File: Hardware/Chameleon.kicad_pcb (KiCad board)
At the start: 2 copper layers, 88 x 88 mm, 72 parts, among them P1 PDI, U1 ATXMEGA16A4U-A, U2 AS1121, U3 TLV71333PDBVR, U4 NCP1402

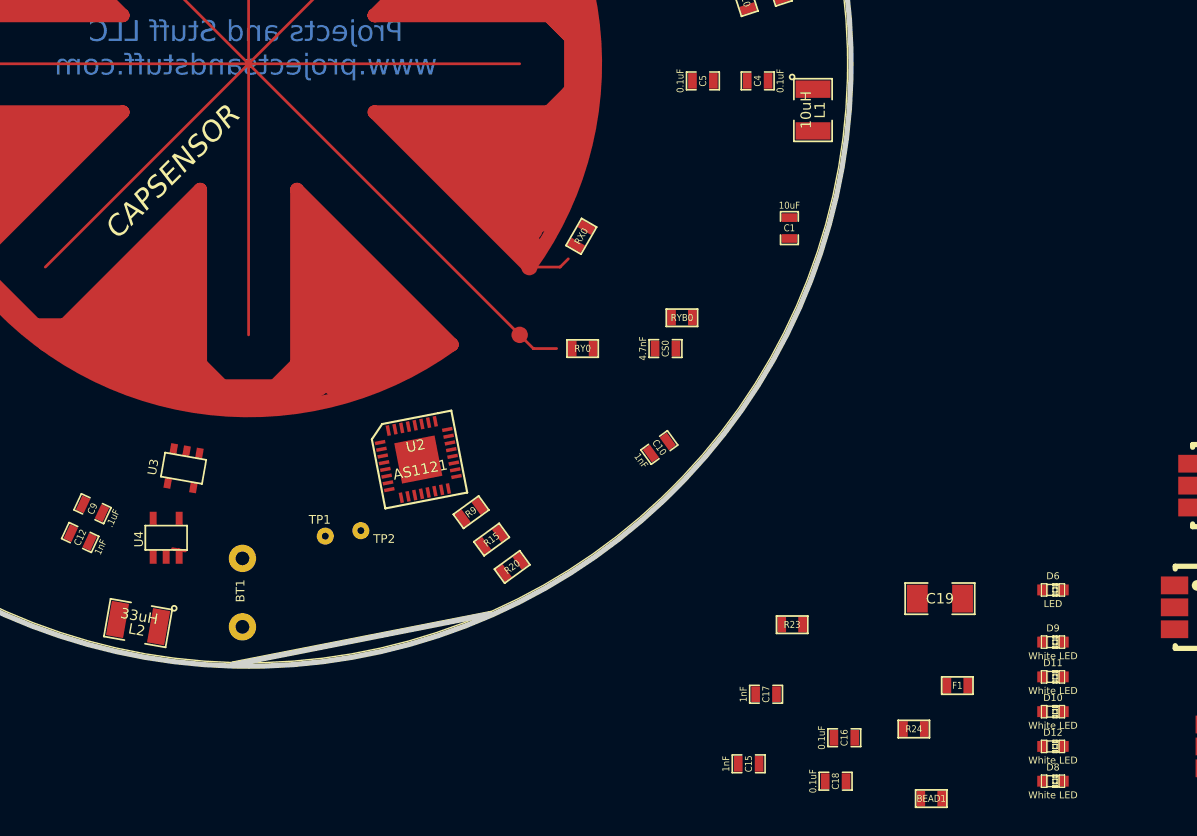
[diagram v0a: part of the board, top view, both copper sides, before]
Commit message: Created netlist and imported components into PCB
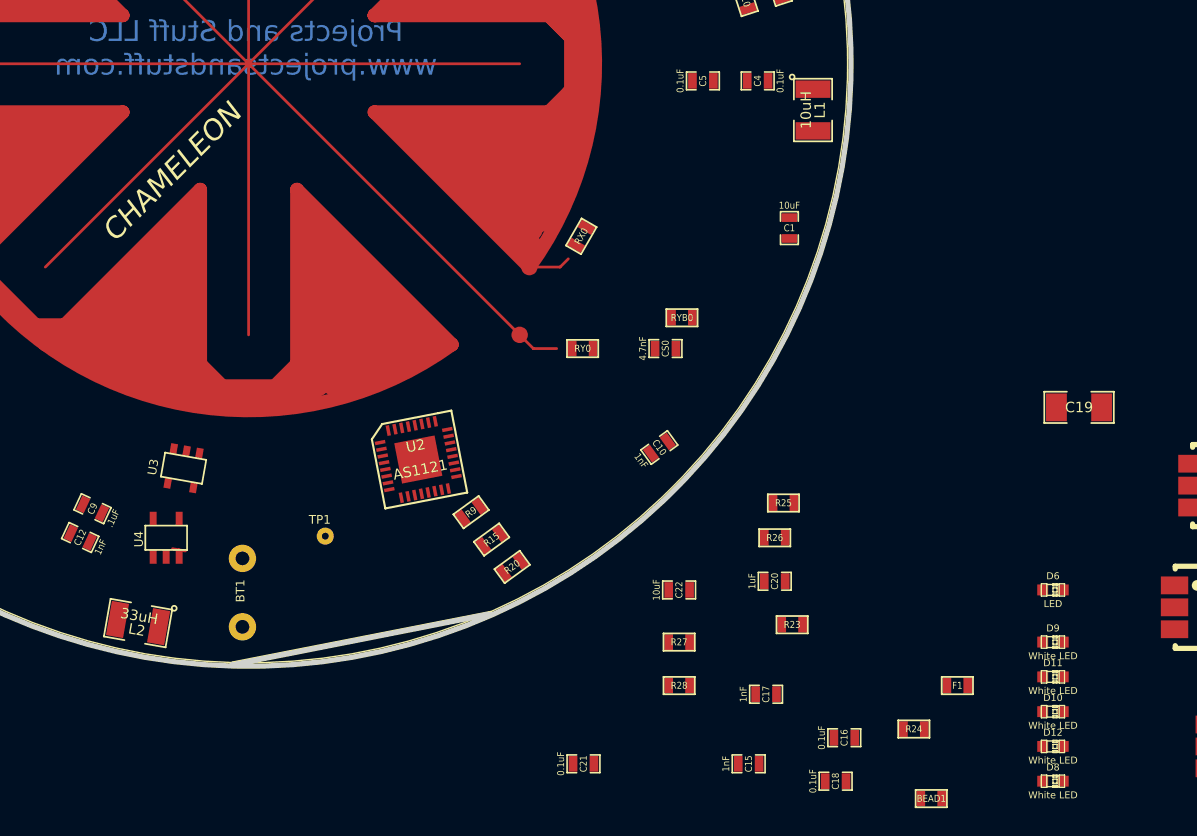
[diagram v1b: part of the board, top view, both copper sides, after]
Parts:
- removed TP2: TST, TestPoint_1-pin
- added C20: 1uF, SM0603_Capa, F.Cu at (138.4, 137.8)
- added C21: 0.1uF, SM0603_Capa, F.Cu at (124.5, 151.1)
- added C22: 10uF, SM0603_Capa, F.Cu at (131.4, 138.4)
- added R25: 10k, SM0603, F.Cu at (139.1, 132.1)
- added R26: 100k, SM0603, F.Cu at (138.4, 134.6)
- added R27: 300k, SM0603, F.Cu at (131.4, 142.2)
- added R28: 100k, SM0603, F.Cu at (131.4, 145.4)
- XOYO1: value CAPSENSOR -> CHAMELEON
- moved C19 17.3 mm to (160.7, 125.1)
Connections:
- BT1 pad 2: N-0000069 -> N-0000047
- C14 pad 1: N-0000069 -> N-0000066
- C16 pad 1: N-0000069 -> N-0000066
- F1 pad 2: N-0000027 -> N-0000047
- L2 pad 1: N-0000069 -> N-0000066
- TP1 pad 1: N-0000069 -> N-0000047
- U3 pad 1: N-0000069 -> N-0000066
- U3 pad 3: N-0000069 -> N-0000066
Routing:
- net (no net): track 0.00 -> 0.95 mm

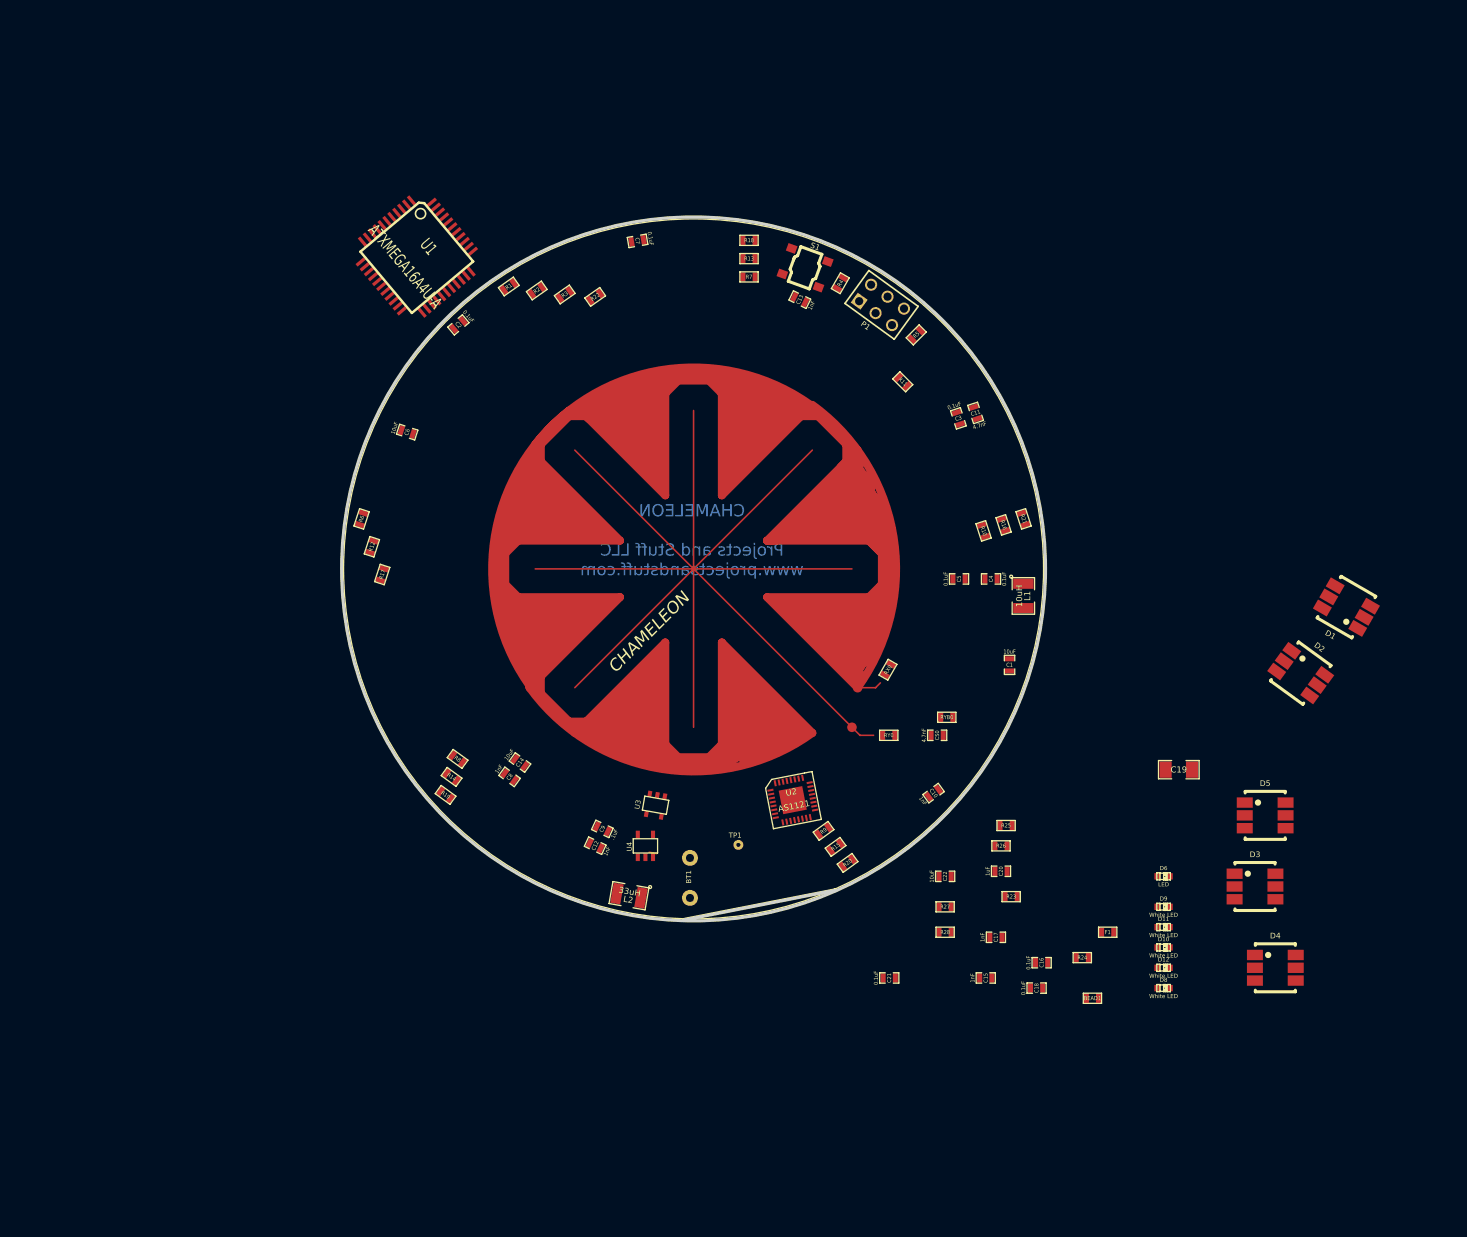
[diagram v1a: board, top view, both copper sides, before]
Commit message: Began grouping components
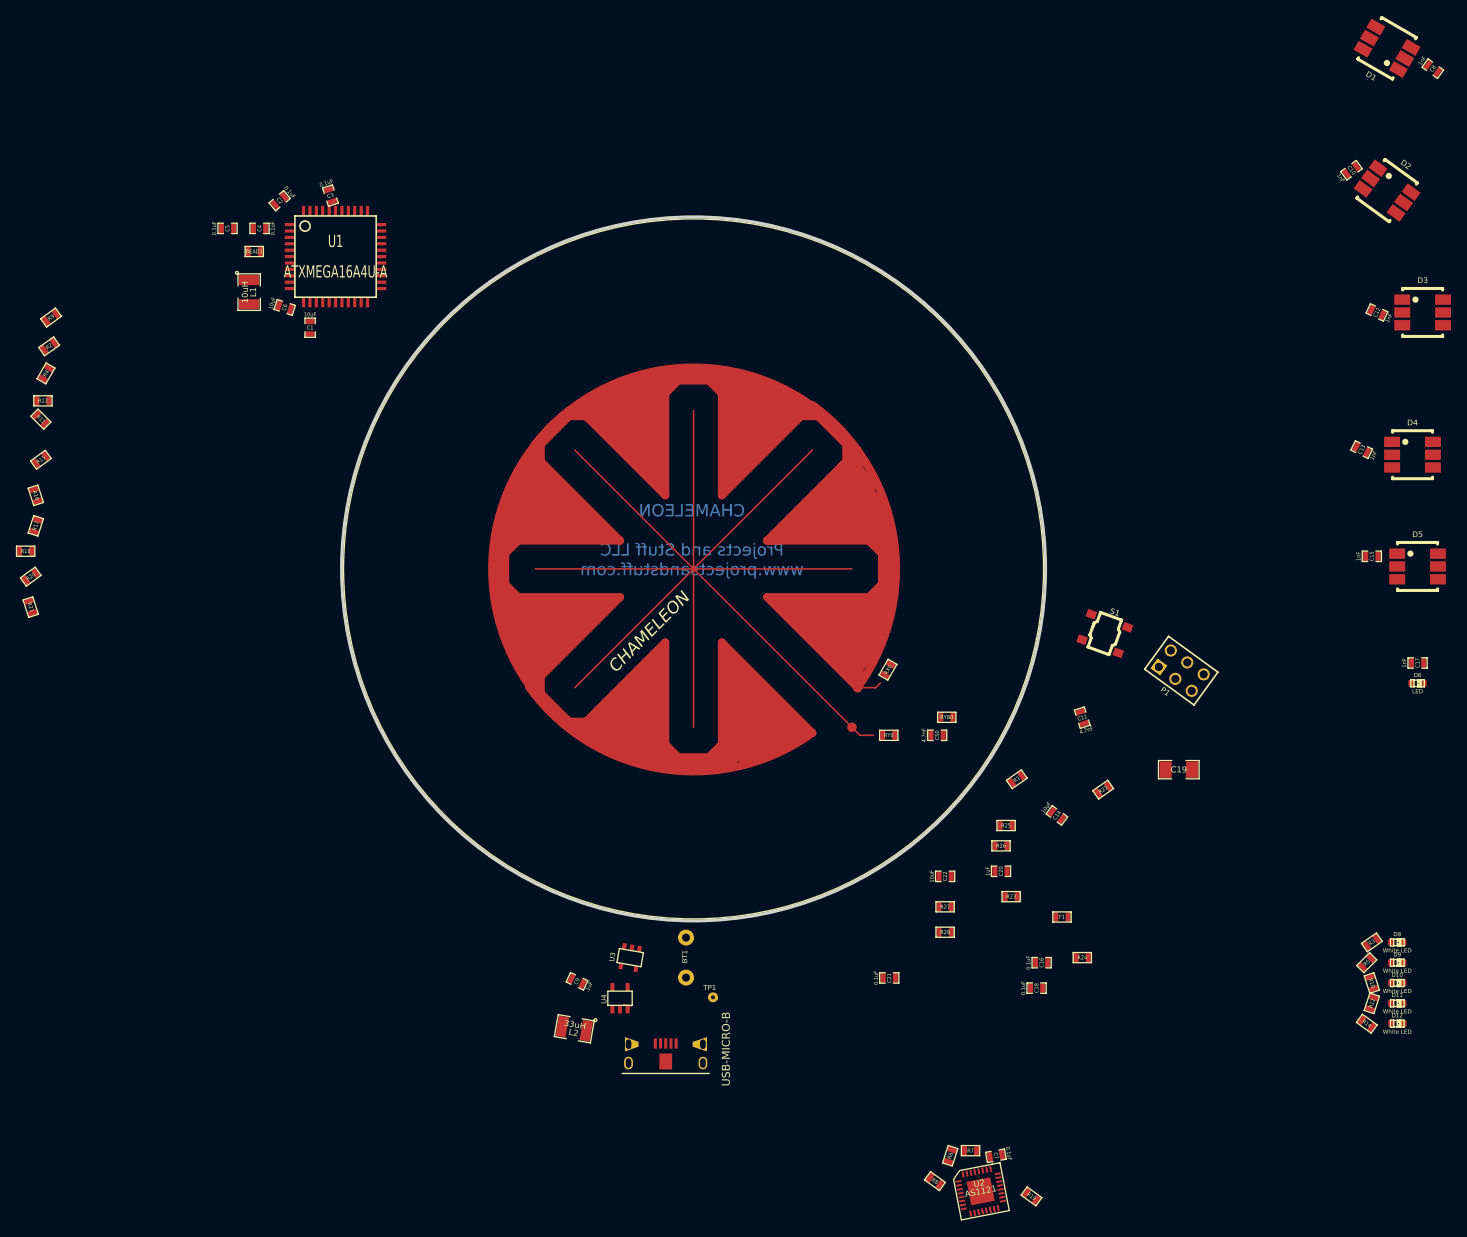
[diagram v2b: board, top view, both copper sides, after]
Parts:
- added J1: USB-MICRO-B, ZX62WRD-B-5PC, F.Cu at (96.5, 160.0)
- U1: footprint TQFP44 -> VQFP44
- moved C8 145.5 mm to (192.4, 37.5)
- moved BEAD1 140.3 mm to (45.1, 60.3)
- moved R12 137.4 mm to (184.8, 154.3)
- moved R3 129.4 mm to (184.8, 146.7)
- moved R21 124.6 mm to (17.1, 104.8)
- moved C7 122.8 mm to (137.8, 173.4)
- moved R16 121.0 mm to (17.8, 90.8)
- moved R14 118.5 mm to (184.2, 156.8)
- moved C12 118.3 mm to (185.4, 67.9)
- moved R9 115.9 mm to (19.7, 68.6)
- moved R7 112.7 mm to (134.6, 172.7)
- moved R15 110.5 mm to (18.4, 86.4)
- moved R6 108.4 mm to (132.1, 173.4)
- moved R20 108.2 mm to (17.1, 101.0)
- moved R11 107.8 mm to (18.4, 81.3)
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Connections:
- net N-0000012 renamed /SHIELD
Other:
- outline, holes or cut-outs redrawn

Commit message: Added VQFN44 and updated XMega chip in PCB
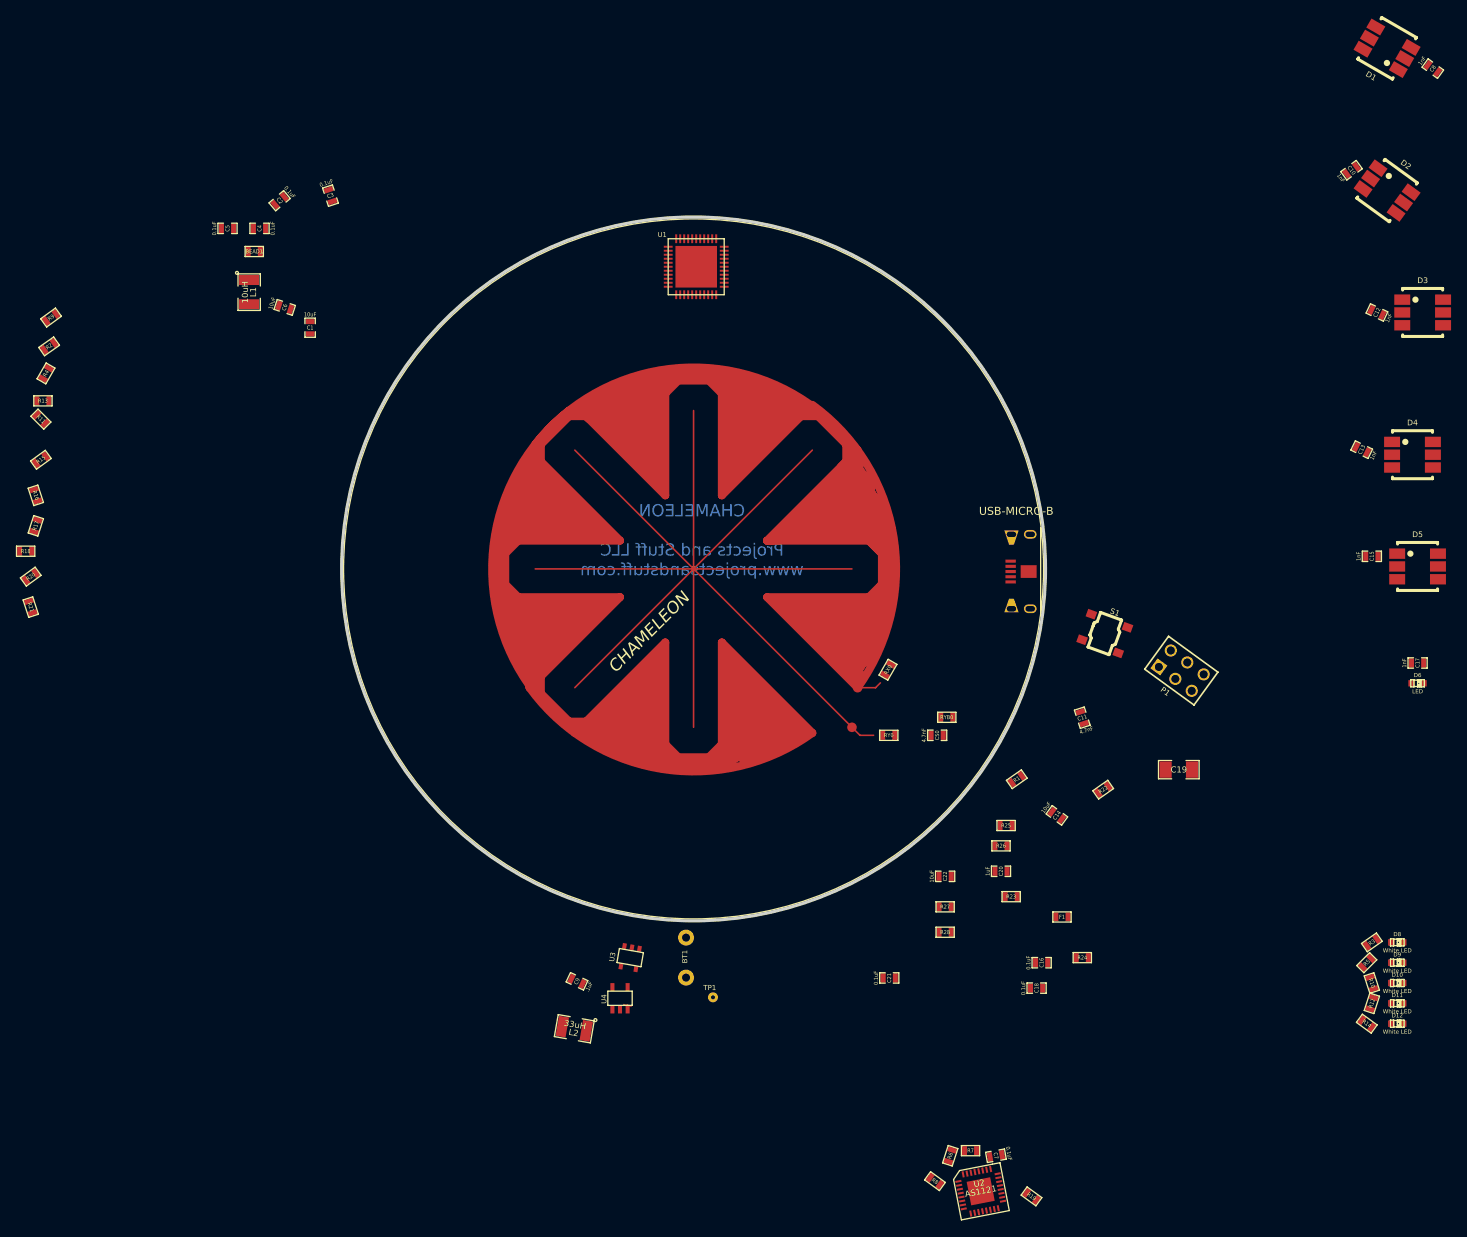
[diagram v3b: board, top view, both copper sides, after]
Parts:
- U1: footprint VQFP44 -> VQFN44
- moved J1 74.0 mm to (140.3, 100.3), turned to 90 degrees
- moved U1 45.1 mm to (100.3, 62.2)

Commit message: Updated XMega with Ground pin and placed several main components
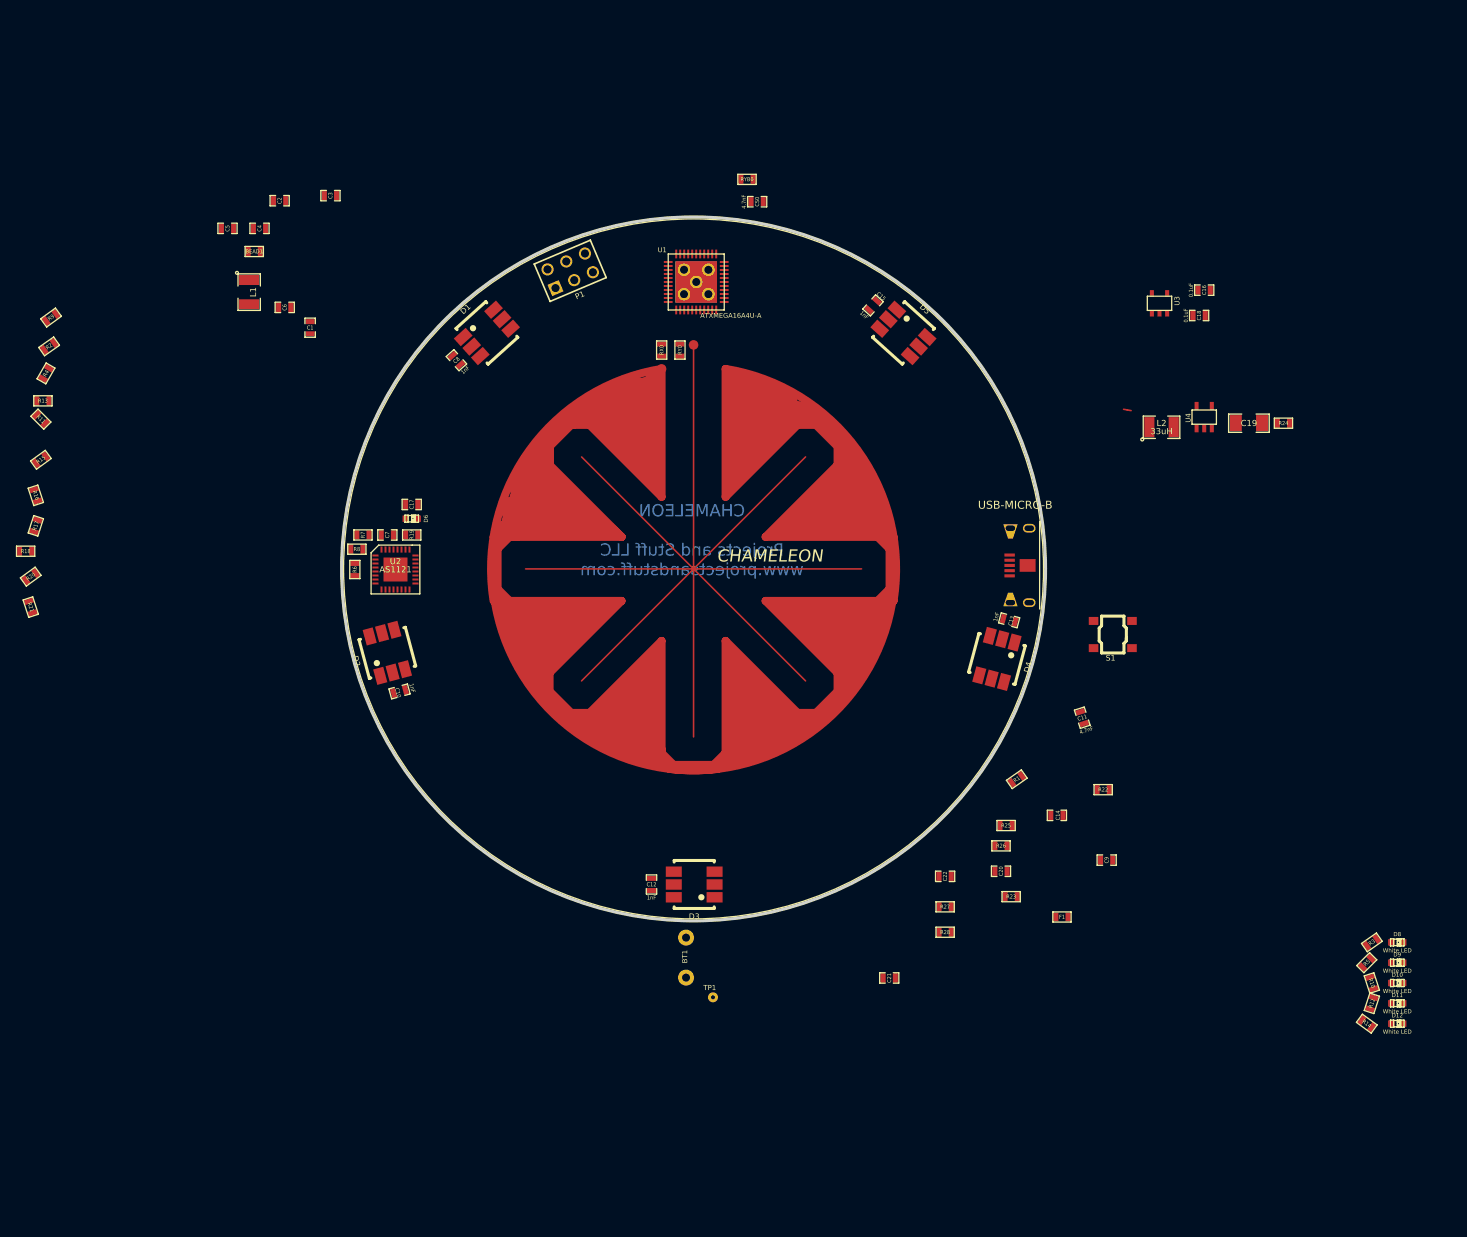
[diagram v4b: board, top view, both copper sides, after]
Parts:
- moved D2 137.7 mm to (61.7, 110.5), turned to 105 degrees
- moved C10 135.7 mm to (63.2, 115.3), turned to 195 degrees
- moved D6 127.4 mm to (64.8, 93.7)
- moved C8 127.4 mm to (70.4, 73.9), turned to 132 degrees
- moved C17 127.3 mm to (64.8, 91.9)
- moved D1 118.0 mm to (74.2, 70.5), turned to 42 degrees
- moved D3 115.8 mm to (100.1, 139.4), turned to 180 degrees
- moved C12 115.5 mm to (94.7, 139.4), turned to 90 degrees
- moved R19 113.3 mm to (64.8, 95.8), turned to 0 degrees
- moved C7 108.7 mm to (61.7, 95.8), turned to 180 degrees
- moved R7 108.1 mm to (58.7, 95.8)
- moved R8 107.1 mm to (57.9, 97.5), turned to 0 degrees
- moved U2 106.7 mm to (62.7, 100.1), turned to 0 degrees
- moved U3 105.2 mm to (158.2, 66.8), turned to 0 degrees
- moved L2 105.1 mm to (158.5, 82.3), turned to 0 degrees
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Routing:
- net N-0000010: track 3.11 -> 0.00 mm
- net N-0000011: track 3.09 -> 0.00 mm
